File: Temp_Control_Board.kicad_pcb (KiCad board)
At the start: 2 copper layers, 111.8 x 50.8 mm, 39 parts, among them J1 OVEN_INTERFACE, J2 OLED, J3 USB_B_Micro, J4 MICROSD, U1 ESP-WROOM-32, U2 AZ1117EH-3.3TRG1, U3 ROTARY_ENC_PEC12R, U4 FT232RLREEL, U5 MAX31855KASA

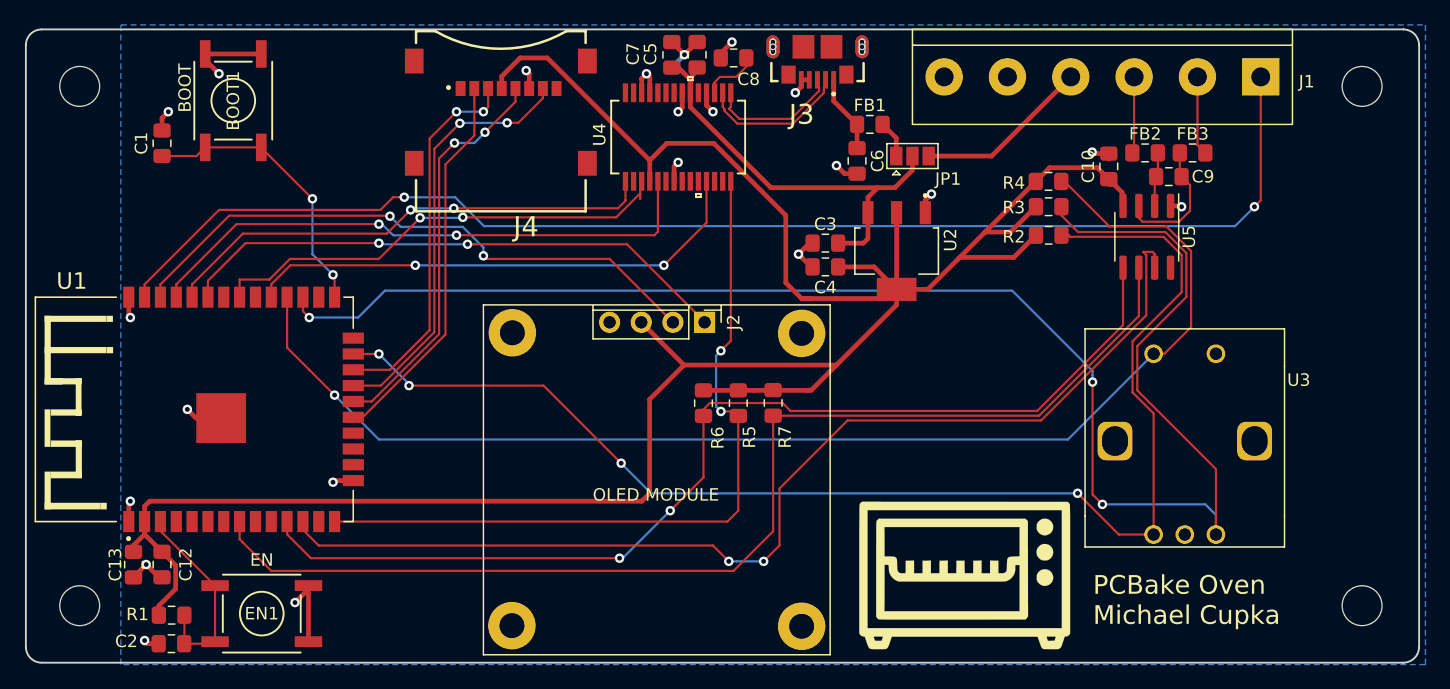
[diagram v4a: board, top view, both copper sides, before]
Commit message: proj: Updated to KiCAD 6
    - removed old files with KiCAD 5 extensions, added new files.
    - added footprint and symbol library tables
    - ignored autosave, cache, and backup data
    - added .gitignore
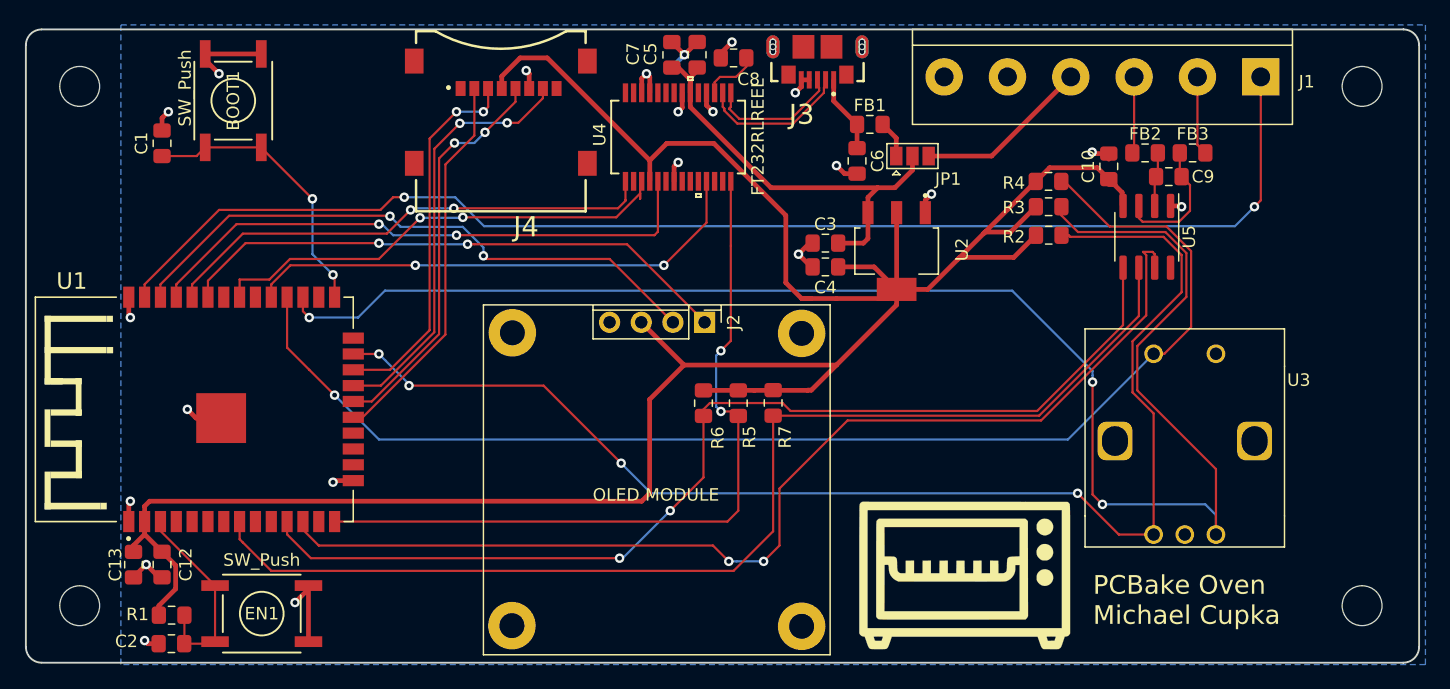
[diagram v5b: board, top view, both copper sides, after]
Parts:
- BOOT1: value BOOT -> SW_Push
- EN1: value EN -> SW_Push
- J4: footprint MICROSD_CONN:GCT_MEM2067-02-180-00-A_REVB -> microsd_connector:GCT_MEM2067-02-180-00-A_REVB
- U2: footprint 3V3_Regulator:SOT230P700X180-4N -> 3V3_regulator:SOT230P700X180-4N
- U4: footprint FT232:FT232RLREEL -> ft232r:FT232RLREEL
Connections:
- J3 pad 6: Net-(J3-Pad6) -> unconnected-(J3-Pad6)
- J4 pad 1: Net-(J4-Pad1) -> unconnected-(J4-Pad1)
- J4 pad 10: (no net) -> unconnected-(J4-Pad10)
- J4 pad 11: (no net) -> unconnected-(J4-Pad10)
- J4 pad 12: (no net) -> unconnected-(J4-Pad10)
- J4 pad 8: Net-(J4-Pad8) -> unconnected-(J4-Pad8)
- J4 pad 9: (no net) -> unconnected-(J4-Pad10)
- U1 pad 10: Net-(U1-Pad10) -> unconnected-(U1-Pad10)
- U1 pad 13: Net-(U1-Pad13) -> unconnected-(U1-Pad13)
- U1 pad 16: Net-(U1-Pad16) -> unconnected-(U1-Pad16)
- U1 pad 17: Net-(U1-Pad17) -> unconnected-(U1-Pad17)
- U1 pad 18: Net-(U1-Pad18) -> unconnected-(U1-Pad18)
- U1 pad 24: Net-(U1-Pad24) -> unconnected-(U1-Pad24)
- U1 pad 26: Net-(U1-Pad26) -> unconnected-(U1-Pad26)
- U1 pad 30: Net-(U1-Pad30) -> unconnected-(U1-Pad30)
- U1 pad 4: Net-(U1-Pad4) -> unconnected-(U1-Pad4)
- U1 pad 5: Net-(U1-Pad5) -> unconnected-(U1-Pad5)
- U1 pad 6: Net-(U1-Pad6) -> unconnected-(U1-Pad6)
- U1 pad 7: Net-(U1-Pad7) -> unconnected-(U1-Pad7)
- U1 pad 9: Net-(U1-Pad9) -> unconnected-(U1-Pad9)
- U4 pad 10: Net-(U4-Pad10) -> unconnected-(U4-Pad10)
- U4 pad 12: Net-(U4-Pad12) -> unconnected-(U4-Pad12)
- U4 pad 13: Net-(U4-Pad13) -> unconnected-(U4-Pad13)
- U4 pad 19: Net-(U4-Pad19) -> unconnected-(U4-Pad19)
- U4 pad 2: Net-(U4-Pad2) -> unconnected-(U4-Pad2)
- U4 pad 22: Net-(U4-Pad22) -> unconnected-(U4-Pad22)
- U4 pad 23: Net-(U4-Pad23) -> unconnected-(U4-Pad23)
- U4 pad 24: Net-(U4-Pad24) -> unconnected-(U4-Pad24)
- U4 pad 27: Net-(U4-Pad27) -> unconnected-(U4-Pad27)
- U4 pad 28: Net-(U4-Pad28) -> unconnected-(U4-Pad28)
- U4 pad 6: Net-(U4-Pad6) -> unconnected-(U4-Pad6)
- U4 pad 8: Net-(U4-Pad8) -> unconnected-(U4-Pad8)
- U4 pad 9: Net-(U4-Pad9) -> unconnected-(U4-Pad9)
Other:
- net class Default removed
- net class Power removed

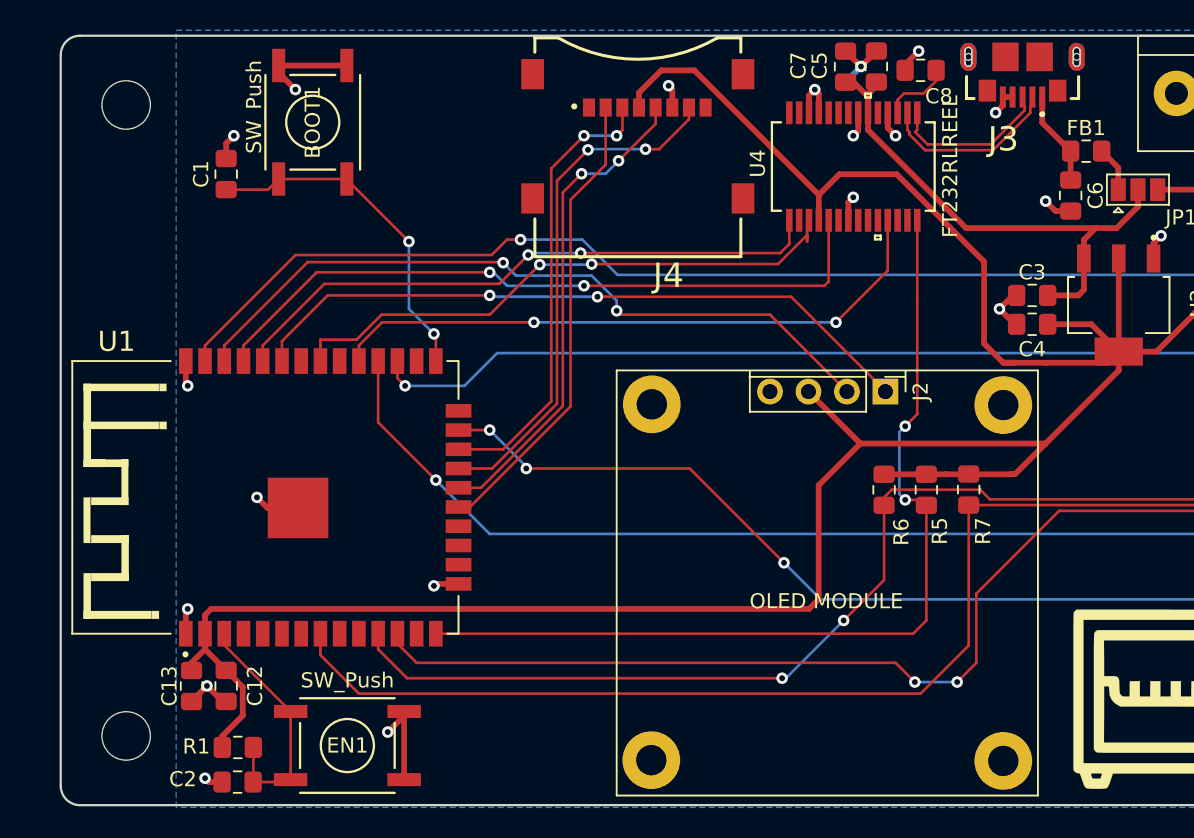
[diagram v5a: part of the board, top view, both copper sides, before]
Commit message: pcb/shc: Fixed tactile switch routing, tied USB shield to GND
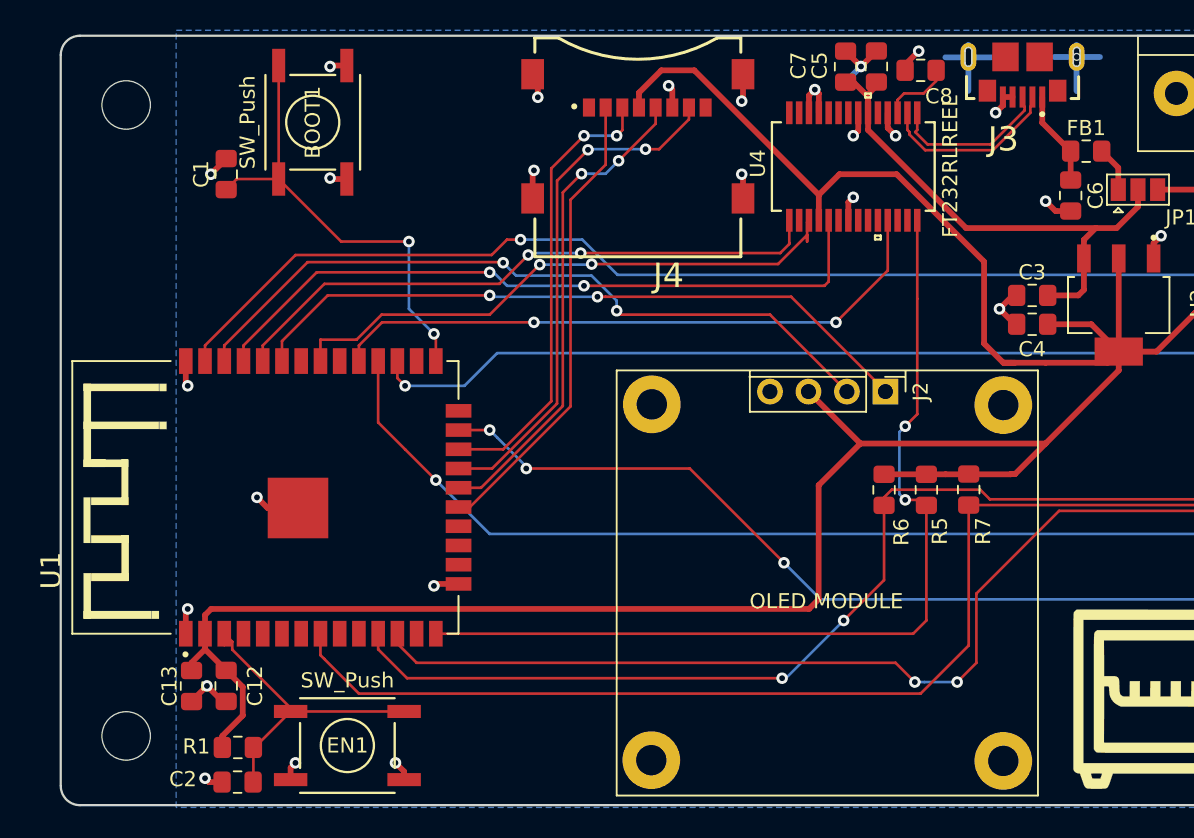
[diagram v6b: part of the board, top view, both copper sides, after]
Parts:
- BOOT1, EN1: footprint TACTILE_SWITCH:PTS645SK43SMTR92LF-CONNECTED -> tactile_switch:PTS645SK43SMTR92LF-CONNECTED
- J3: footprint USB_CONNECTOR:GCT_USB3076-XX-X_REVC -> usb_connector:GCT_USB3076-XX-X_REVC
- U1: footprint ESP32:MODULE_ESP-WROOM-32 -> esp32:MODULE_ESP-WROOM-32
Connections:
- J3 pad 6: unconnected-(J3-Pad6) -> GND
- J4 pad 10: unconnected-(J4-Pad10) -> GND
- J4 pad 11: unconnected-(J4-Pad10) -> GND
- J4 pad 12: unconnected-(J4-Pad10) -> GND
- J4 pad 9: unconnected-(J4-Pad10) -> GND
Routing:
- net GND: track 53.2 -> 64.1 mm, vias 22 -> 28
- net BOOT: track 22.7 -> 30.2 mm
- net EN: track 17.0 -> 21.7 mm

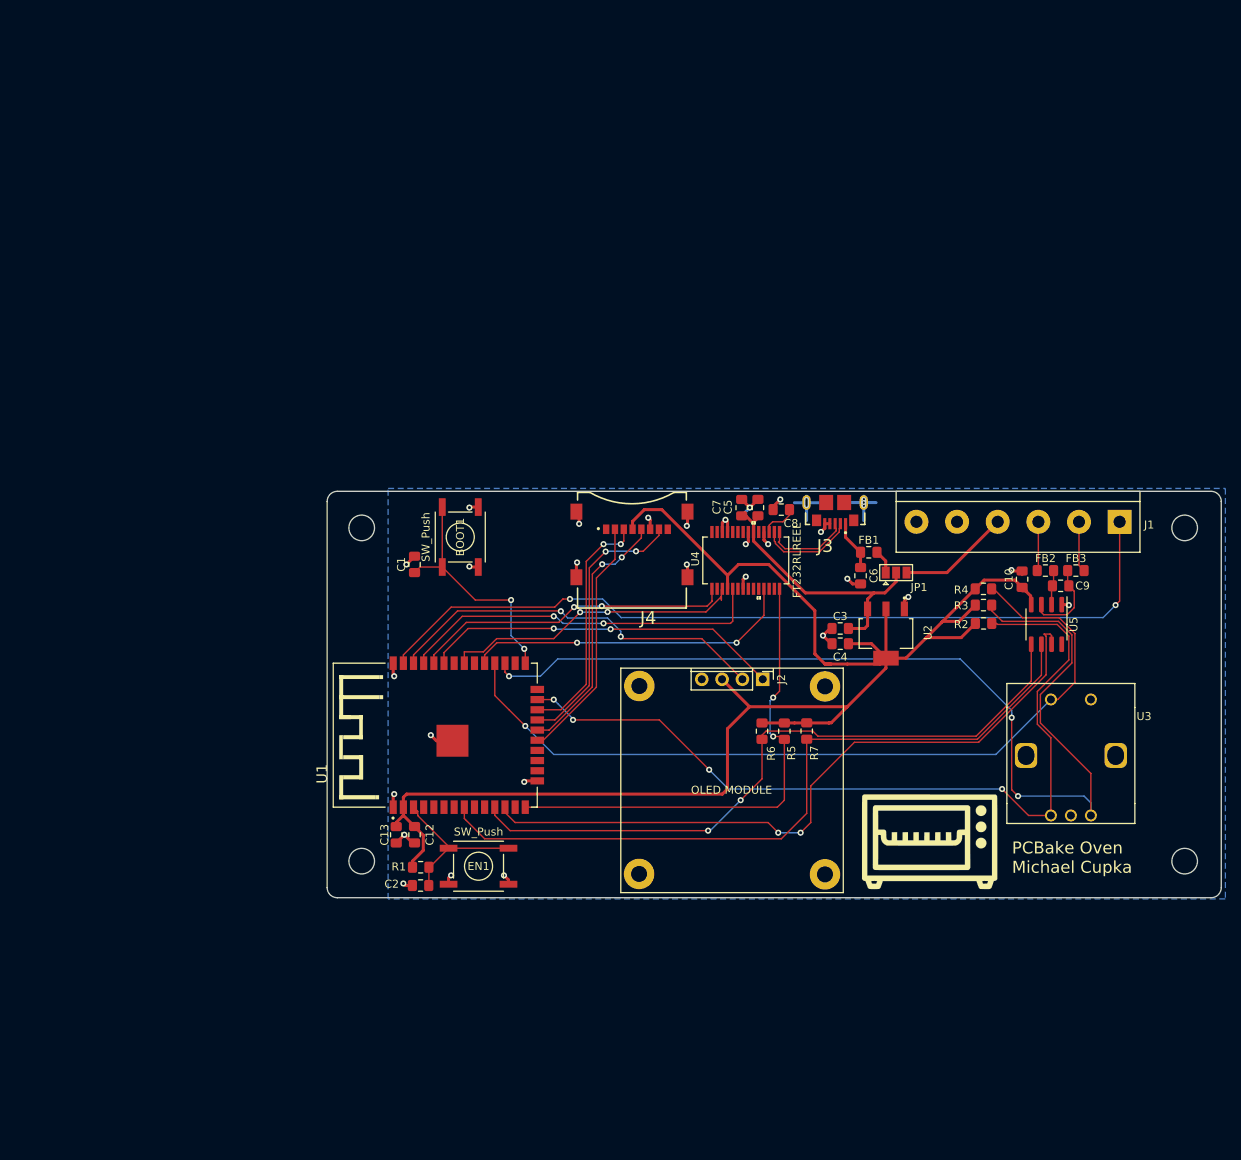
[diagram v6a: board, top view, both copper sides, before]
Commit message: pcb: began re-routing pcb following fixes
    - Switched to much smaller, 4-layer board
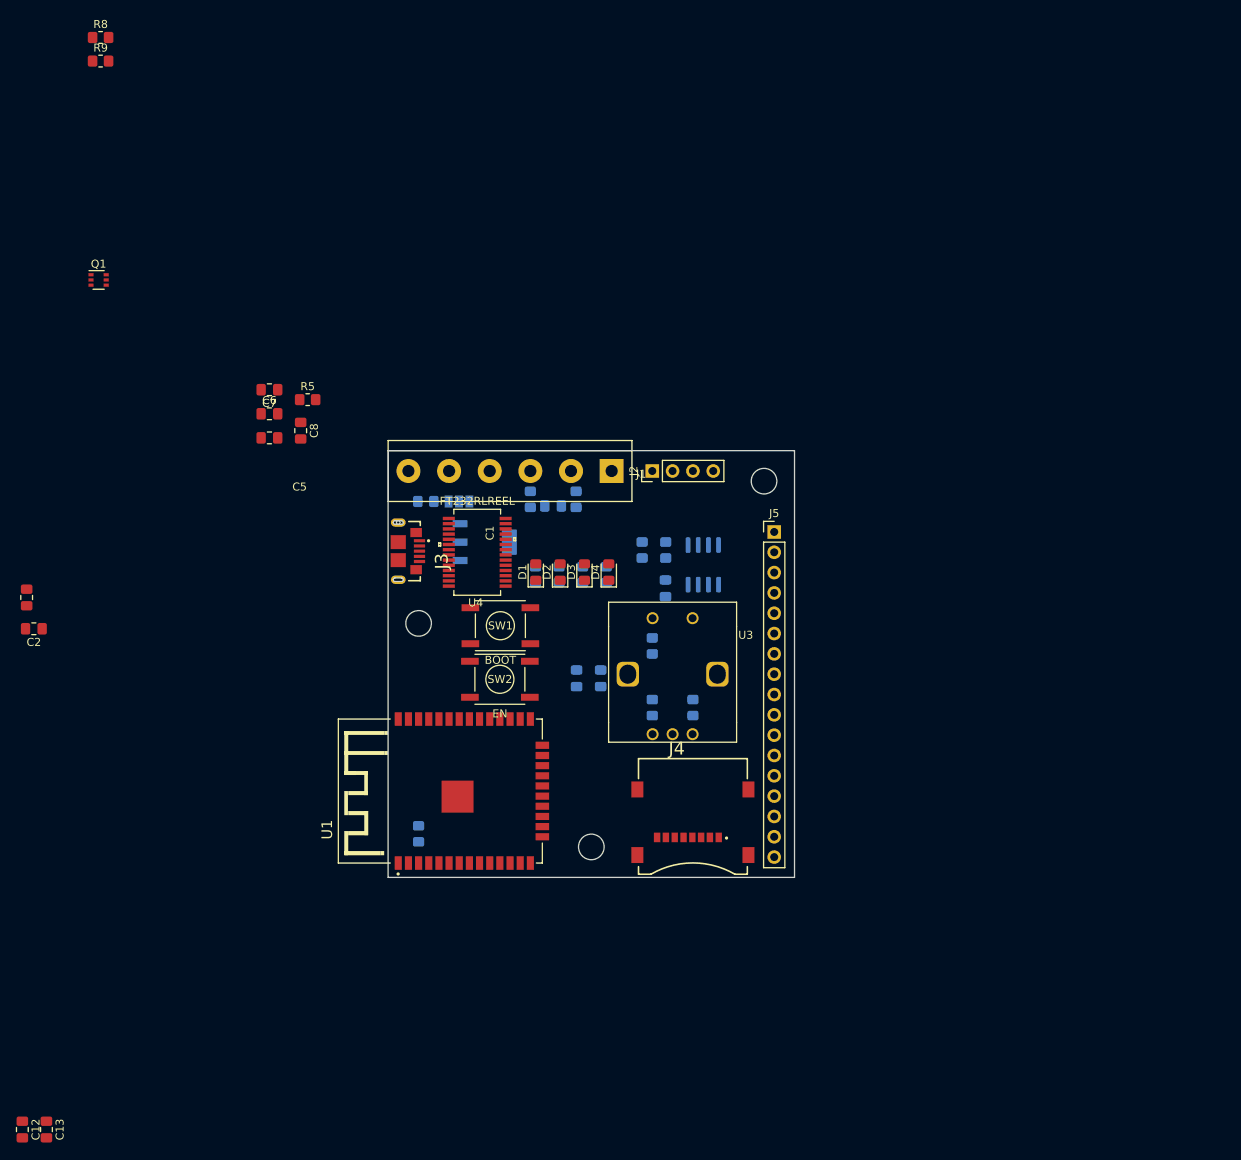
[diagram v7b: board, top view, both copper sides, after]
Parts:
- removed the REF** at (175.8, 150.4)
- added D1: LED_3V3, LED_SMD:LED_0805_2012Metric_Pad1.15x1.40mm_HandSolder, F.Cu at (94.7, 114.2)
- added D2: LED_ESP0, LED_SMD:LED_0805_2012Metric_Pad1.15x1.40mm_HandSolder, F.Cu at (97.7, 114.2)
- added D3: LED_OVEN, LED_SMD:LED_0805_2012Metric_Pad1.15x1.40mm_HandSolder, F.Cu at (100.7, 114.2)
- added D4: LED_ESP1, LED_SMD:LED_0805_2012Metric_Pad1.15x1.40mm_HandSolder, F.Cu at (103.8, 114.2)
- added J5: BREAKOUT, Connector_PinHeader_2.54mm:PinHeader_1x17_P2.54mm_Vertical, F.Cu at (124.5, 109.2)
- added Q1: BC847BS, Package_TO_SOT_SMD:SOT-363_SC-70-6, F.Cu at (40.0, 77.7)
- added R10: 1K, Resistor_SMD:R_0805_2012Metric_Pad1.20x1.40mm_HandSolder, B.Cu at (103.5, 114.6)
- added R11: 1K, Resistor_SMD:R_0805_2012Metric_Pad1.20x1.40mm_HandSolder, B.Cu at (100.5, 114.6)
- added R12: 1K, Resistor_SMD:R_0805_2012Metric_Pad1.20x1.40mm_HandSolder, B.Cu at (97.6, 114.6)
- added R13: 1K, Resistor_SMD:R_0805_2012Metric_Pad1.20x1.40mm_HandSolder, B.Cu at (94.6, 114.6)
- added R8: 10K, Resistor_SMD:R_0805_2012Metric_Pad1.20x1.40mm_HandSolder, F.Cu at (40.3, 47.4)
- added R9: 10K, Resistor_SMD:R_0805_2012Metric_Pad1.20x1.40mm_HandSolder, F.Cu at (40.3, 50.4)
- C1, C12: value .1uF -> 100nF; footprint Capacitor_SMD:C_0805_2012Metric_Pad1.15x1.40mm_HandSolder -> Capacitor_SMD:C_0805_2012Metric_Pad1.18x1.45mm_HandSolder
- C10, C3, C4, C9: footprint Capacitor_SMD:C_0805_2012Metric_Pad1.15x1.40mm_HandSolder -> Capacitor_SMD:C_0805_2012Metric_Pad1.18x1.45mm_HandSolder; moved to B.Cu
- C13, C5, C6, C7, C8: footprint Capacitor_SMD:C_0805_2012Metric_Pad1.15x1.40mm_HandSolder -> Capacitor_SMD:C_0805_2012Metric_Pad1.18x1.45mm_HandSolder
- C2: value .1uF -> 1uF; footprint Capacitor_SMD:C_0805_2012Metric_Pad1.15x1.40mm_HandSolder -> Capacitor_SMD:C_0805_2012Metric_Pad1.18x1.45mm_HandSolder
- FB1, FB2, FB3, R1, R2, R3, R4, R6, R7: footprint Resistor_SMD:R_0805_2012Metric_Pad1.15x1.40mm_HandSolder -> Resistor_SMD:R_0805_2012Metric_Pad1.20x1.40mm_HandSolder; moved to B.Cu
- G***, JP1, U2, U5: moved to B.Cu
- J2: footprint Display:OLED_1MIL_HEADER_WHOLES -> Connector_PinHeader_2.54mm:PinHeader_1x04_P2.54mm_Vertical
- R5: footprint Resistor_SMD:R_0805_2012Metric_Pad1.15x1.40mm_HandSolder -> Resistor_SMD:R_0805_2012Metric_Pad1.20x1.40mm_HandSolder
- SW1: renamed from BOOT1; value SW_Push -> BOOT
- SW2: renamed from EN1; value SW_Push -> EN
- moved C6 76.6 mm to (61.4, 94.5), turned to 0 degrees
- moved R5 72.6 mm to (66.1, 92.7), turned to 0 degrees
- moved FB2 65.0 mm to (94.0, 105.1), turned to 90 degrees
- moved C9 64.2 mm to (96.8, 106.0)
- moved J1 63.8 mm to (104.1, 101.6)
- moved FB3 63.1 mm to (99.7, 105.1), turned to 90 degrees
- moved C5 61.7 mm to (61.4, 97.5), turned to 180 degrees
- moved C12 61.3 mm to (30.5, 183.9)
- moved C8 60.9 mm to (65.3, 96.6), turned to -90 degrees
- moved C7 60.8 mm to (61.4, 91.4), turned to 180 degrees
- moved C2 58.0 mm to (31.9, 121.3)
- moved G*** 57.7 mm to (86.3, 144.8), turned to 180 degrees
- moved C13 57.2 mm to (33.5, 183.9)
- moved FB1 55.7 mm to (80.9, 105.4)
- moved JP1 55.4 mm to (85.1, 105.4)
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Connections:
- U1 pad 10: unconnected-(U1-Pad10) -> RELAY+
- U1 pad 19: SD_CS -> unconnected-(U1-SCS/CMD-Pad19)
- U1 pad 20: SD_SCK -> unconnected-(U1-SCK/CLK-Pad20)
- U1 pad 21: SD_DO -> unconnected-(U1-SDO/SD0-Pad21)
- U1 pad 22: SD_DI -> unconnected-(U1-SDI/SD1-Pad22)
- U1 pad 24: unconnected-(U1-Pad24) -> LED_ESP0
- U1 pad 26: unconnected-(U1-Pad26) -> LED_ESP1
- U1 pad 29: FT_CTS -> SD_CS
- U1 pad 30: unconnected-(U1-Pad30) -> SD_SCK
- U1 pad 31: FT_RTS -> SD_DI
- U1 pad 37: RELAY+ -> SD_DO
- U4 pad 11: FT_CTS -> unconnected-(U4-CTS#-Pad11)
- U4 pad 2: unconnected-(U4-Pad2) -> FT_DTR
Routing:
- net +3V3: track 199.0 -> 0.00 mm
- net ROT_CHB: track 129.1 -> 0.00 mm, vias 3 -> 0
- net RELAY+: track 105.4 -> 0.00 mm, vias 2 -> 0
- net ROT_CHA: track 105.3 -> 0.00 mm, vias 4 -> 0
- net ROT_SW1: track 102.2 -> 0.00 mm, vias 1 -> 0
- net MAX_CSN: track 92.4 -> 0.00 mm
- net MAX_SO: track 87.5 -> 0.00 mm, vias 2 -> 0
- net MAX_SCK: track 85.0 -> 0.00 mm, vias 2 -> 0
- net GND: track 64.1 -> 0.00 mm, vias 28 -> 0
- net FT_PWREN: track 61.4 -> 0.00 mm, vias 2 -> 0
- net OLED_SCL: track 48.8 -> 0.00 mm, vias 2 -> 0
- net FT_RX: track 46.2 -> 0.00 mm, vias 2 -> 0
- net OLED_SDA: track 45.1 -> 0.00 mm, vias 2 -> 0
- net FT_CTS: track 41.3 -> 0.00 mm, vias 2 -> 0
- net FT_TX: track 40.1 -> 0.00 mm, vias 2 -> 0
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- added copper zone on In1.Cu, net GND
- removed copper zone on B.Cu, net GND
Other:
- board size 111.8 x 50.8 mm -> 50.8 x 53.3 mm
- copper layers 2 -> 4
